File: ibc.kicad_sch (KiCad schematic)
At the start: 36 parts, among them U3 EPC23104

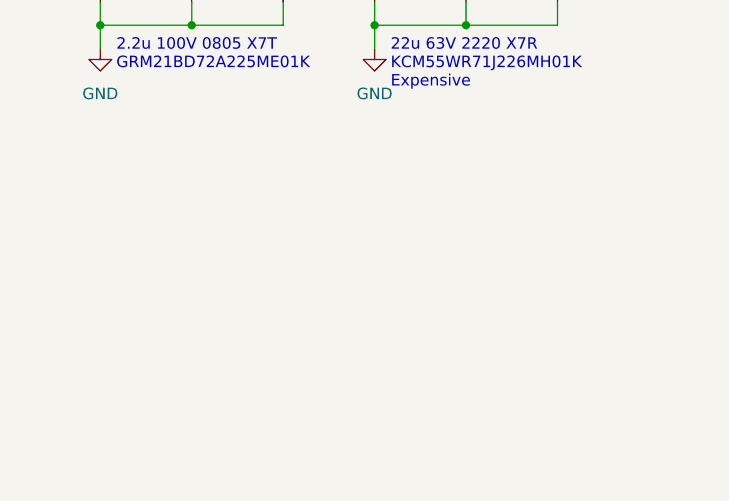
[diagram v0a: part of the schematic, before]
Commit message: reorg and add 10MHz
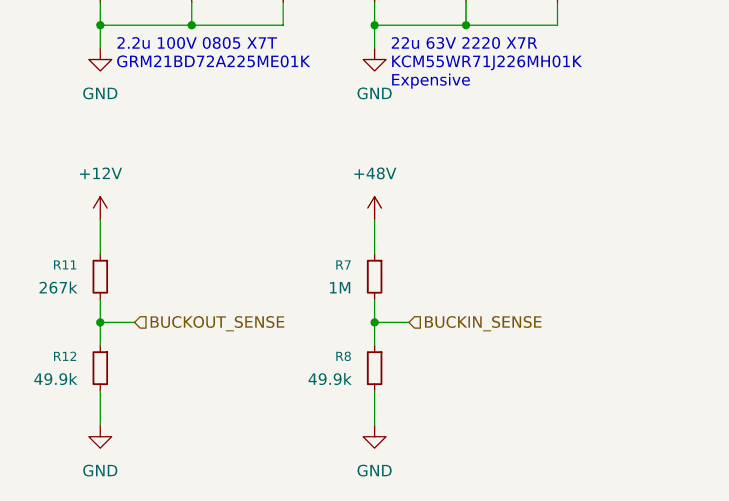
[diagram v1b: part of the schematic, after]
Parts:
- added R11: 267k, Resistor_SMD:R_0402_1005Metric, symbol Device:R_Small
- added R12, R8: 49.9k, Resistor_SMD:R_0402_1005Metric, symbol Device:R_Small
- added R7: 1M, Resistor_SMD:R_0402_1005Metric, symbol Device:R_Small
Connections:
- net +12V: now also R11.1
- net +48V: now also R7.1
- net GND: now also R12.2, R8.2
- new net BUCKIN_SENSE: R7.2, R8.1
- new net BUCKOUT_SENSE: R11.2, R12.1

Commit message: Renumber refdes
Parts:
- renumbered C7 to C1, C16 to C10, C17 to C11, C18 to C12, C19 to C13, C20 to C14, C21 to C15, C22 to C16, C23 to C17, C24 to C18, C25 to C19, C8 to C2, C26 to C20, C27 to C21, C28 to C22, C29 to C23, C30 to C24, C31 to C25, C32 to C26, C33 to C27, C9 to C3, C10 to C4, C11 to C5, C12 to C6, C13 to C7, C14 to C8, C15 to C9, L2 to L1, R22 to R10, R23 to R11, R24 to R12, R11 to R3, R12 to R4, R7 to R5, R8 to R6, R19 to R7, R20 to R8, R21 to R9, U3 to U1
